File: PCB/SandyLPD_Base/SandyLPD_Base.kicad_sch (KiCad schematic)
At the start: 230 parts, among them J1 Conn_02x02_Odd_Even, J10 Conn_01x10_Pin, J11 Conn_01x03, J2 Conn_01x03, J4 Conn_01x10_Pin, J5 USB_C_Receptacle_USB2.0, J6 USB_C_Receptacle_USB2.0, J7 USB_C_Receptacle_USB2.0, J8 USB_C_Receptacle_USB2.0, J9 Conn_02x02_Odd_Even, SW1 BOOT_ALT, SW2 RESET_ALT, SW3 SW_DIP_x04, SW4 BOOT_ALT, SW5 RESET_ALT, SW6 SW_DIP_x04, U1 NCP1117-3.3_SOT223, U2 NCP1117-3.3_SOT223, U3 RP2040, U4 W25Q128JVPIQ, U5 RP2040, U6 W25Q128JVPIQ, Y1 12MHz, Y2 12MHz

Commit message: ネジ等の3Dモデル追加
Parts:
- H_btm_1, H_btm_2, H_btm_3, H_btm_4, H_btm_5, H_btm_6: footprint locallib:MountingHole_M2_Through-hole_tap_THC-0.8-x-2 -> locallib:MountingHole_M2_Through-hole_tap_THC-0.8-1.0-2
- H_mid_1, H_mid_10, H_mid_11, H_mid_12, H_mid_13, H_mid_14, H_mid_15, H_mid_16, H_mid_17, H_mid_18, H_mid_19, H_mid_2, H_mid_20, H_mid_21, H_mid_22, H_mid_3, H_mid_4, H_mid_5, H_mid_6, H_mid_7, H_mid_8, H_mid_9: footprint locallib:MountingHole_M2_Through-hole_tap_THC-0.8-x-2 -> locallib:MountingHole_M2_Through-hole_tap_THC-0.8-2.0-2
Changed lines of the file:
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@@
 			)
 		)
-		(property "Footprint" "locallib:MountingHole_M2_Through-hole_tap_THC-0.8-x-2"
+		(property "Footprint" "locallib:MountingHole_M2_Through-hole_tap_THC-0.8-2.0-2"
 			(at 196.215 311.785 0)
 			(effects
@@
 			)
 		)
-		(property "Footprint" "locallib:MountingHole_M2_Through-hole_tap_THC-0.8-x-2"
+		(property "Footprint" "locallib:MountingHole_M2_Through-hole_tap_THC-0.8-1.0-2"
 			(at 89.535 311.15 0)
 			(effects
@@
 			)
 		)
-		(property "Footprint" "locallib:MountingHole_M2_Through-hole_tap_THC-0.8-x-2"
+		(property "Footprint" "locallib:MountingHole_M2_Through-hole_tap_THC-0.8-2.0-2"
 			(at 264.795 311.785 0)
 			(effects
@@
 			)
 		)
-		(property "Footprint" "locallib:MountingHole_M2_Through-hole_tap_THC-0.8-x-2"
+		(property "Footprint" "locallib:MountingHole_M2_Through-hole_tap_THC-0.8-2.0-2"
 			(at 347.345 332.105 0)
 			(effects
@@
 			)
 		)
-		(property "Footprint" "locallib:MountingHole_M2_Through-hole_tap_THC-0.8-x-2"
+		(property "Footprint" "locallib:MountingHole_M2_Through-hole_tap_THC-0.8-2.0-2"
 			(at 342.265 311.785 0)
 			(effects
@@
 			)
 		)
-		(property "Footprint" "locallib:MountingHole_M2_Through-hole_tap_THC-0.8-x-2"
+		(property "Footprint" "locallib:MountingHole_M2_Through-hole_tap_THC-0.8-2.0-2"
 			(at 422.275 311.785 0)
 			(effects
@@
 			)
 		)
-		(property "Footprint" "locallib:MountingHole_M2_Through-hole_tap_THC-0.8-x-2"
+		(property "Footprint" "locallib:MountingHole_M2_Through-hole_tap_THC-0.8-2.0-2"
 			(at 422.275 321.945 0)
 			(effects
@@
 			)
 		)
-		(property "Footprint" "locallib:MountingHole_M2_Through-hole_tap_THC-0.8-x-2"
+		(property "Footprint" "locallib:MountingHole_M2_Through-hole_tap_THC-0.8-2.0-2"
 			(at 196.215 321.945 0)
 			(effects
@@
 			)
 		)
-		(property "Footprint" "locallib:MountingHole_M2_Through-hole_tap_THC-0.8-x-2"
+		(property "Footprint" "locallib:MountingHole_M2_Through-hole_tap_THC-0.8-1.0-2"
 			(at 39.37 323.85 0)
 			(effects
@@
 			)
 		)
-		(property "Footprint" "locallib:MountingHole_M2_Through-hole_tap_THC-0.8-x-2"
+		(property "Footprint" "locallib:MountingHole_M2_Through-hole_tap_THC-0.8-1.0-2"
 			(at 100.965 323.85 0)
 			(effects
@@
 			)
 		)
-		(property "Footprint" "locallib:MountingHole_M2_Through-hole_tap_THC-0.8-x-2"
+		(property "Footprint" "locallib:MountingHole_M2_Through-hole_tap_THC-0.8-2.0-2"
 			(at 219.075 321.945 0)
 			(effects
@@
 			)
 		)
-		(property "Footprint" "locallib:MountingHole_M2_Through-hole_tap_THC-0.8-x-2"
+		(property "Footprint" "locallib:MountingHole_M2_Through-hole_tap_THC-0.8-2.0-2"
 			(at 244.475 311.785 0)
 			(effects
@@
 			)
 		)
-		(property "Footprint" "locallib:MountingHole_M2_Through-hole_tap_THC-0.8-x-2"
+		(property "Footprint" "locallib:MountingHole_M2_Through-hole_tap_THC-0.8-2.0-2"
 			(at 283.21 321.945 0)
 			(effects
@@
 			)
 		)
-		(property "Footprint" "locallib:MountingHole_M2_Through-hole_tap_THC-0.8-x-2"
+		(property "Footprint" "locallib:MountingHole_M2_Through-hole_tap_THC-0.8-2.0-2"
 			(at 399.415 311.785 0)
 			(effects
@@
 			)
 		)
-		(property "Footprint" "locallib:MountingHole_M2_Through-hole_tap_THC-0.8-x-2"
+		(property "Footprint" "locallib:MountingHole_M2_Through-hole_tap_THC-0.8-2.0-2"
 			(at 342.265 342.265 0)
 			(effects
@@
 			)
 		)
-		(property "Footprint" "locallib:MountingHole_M2_Through-hole_tap_THC-0.8-x-2"
+		(property "Footprint" "locallib:MountingHole_M2_Through-hole_tap_THC-0.8-1.0-2"
 			(at 10.16 323.85 0)
 			(effects
@@
 			)
 		)
-		(property "Footprint" "locallib:MountingHole_M2_Through-hole_tap_THC-0.8-x-2"
+		(property "Footprint" "locallib:MountingHole_M2_Through-hole_tap_THC-0.8-2.0-2"
 			(at 278.13 332.105 0)
 			(effects
@@
 			)
 		)
-		(property "Footprint" "locallib:MountingHole_M2_Through-hole_tap_THC-0.8-x-2"
+		(property "Footprint" "locallib:MountingHole_M2_Through-hole_tap_THC-0.8-2.0-2"
 			(at 375.285 321.945 0)
 			(effects
@@
 			)
 		)
-		(property "Footprint" "locallib:MountingHole_M2_Through-hole_tap_THC-0.8-x-2"
+		(property "Footprint" "locallib:MountingHole_M2_Through-hole_tap_THC-0.8-2.0-2"
 			(at 219.075 311.785 0)
 			(effects
@@
 			)
 		)
-		(property "Footprint" "locallib:MountingHole_M2_Through-hole_tap_THC-0.8-x-2"
+		(property "Footprint" "locallib:MountingHole_M2_Through-hole_tap_THC-0.8-2.0-2"
 			(at 363.22 311.785 0)
 			(effects
@@
 			)
 		)
-		(property "Footprint" "locallib:MountingHole_M2_Through-hole_tap_THC-0.8-x-2"
+		(property "Footprint" "locallib:MountingHole_M2_Through-hole_tap_THC-0.8-1.0-2"
 			(at 21.59 311.15 0)
 			(effects
@@
 			)
 		)
-		(property "Footprint" "locallib:MountingHole_M2_Through-hole_tap_THC-0.8-x-2"
+		(property "Footprint" "locallib:MountingHole_M2_Through-hole_tap_THC-0.8-2.0-2"
 			(at 399.415 321.945 0)
 			(effects
@@
 			)
 		)
-		(property "Footprint" "locallib:MountingHole_M2_Through-hole_tap_THC-0.8-x-2"
+		(property "Footprint" "locallib:MountingHole_M2_Through-hole_tap_THC-0.8-2.0-2"
 			(at 283.21 342.265 0)
 			(effects
@@
 			)
 		)
-		(property "Footprint" "locallib:MountingHole_M2_Through-hole_tap_THC-0.8-x-2"
+		(property "Footprint" "locallib:MountingHole_M2_Through-hole_tap_THC-0.8-2.0-2"
 			(at 342.265 321.945 0)
 			(effects
@@
 			)
 		)
-		(property "Footprint" "locallib:MountingHole_M2_Through-hole_tap_THC-0.8-x-2"
+		(property "Footprint" "locallib:MountingHole_M2_Through-hole_tap_THC-0.8-1.0-2"
 			(at 71.12 323.85 0)
 			(effects
@@
 			)
 		)
-		(property "Footprint" "locallib:MountingHole_M2_Through-hole_tap_THC-0.8-x-2"
+		(property "Footprint" "locallib:MountingHole_M2_Through-hole_tap_THC-0.8-2.0-2"
 			(at 377.825 311.785 0)
 			(effects
@@
 			)
 		)
-		(property "Footprint" "locallib:MountingHole_M2_Through-hole_tap_THC-0.8-x-2"
+		(property "Footprint" "locallib:MountingHole_M2_Through-hole_tap_THC-0.8-2.0-2"
 			(at 283.21 311.785 0)
 			(effects
@@
 			)
 		)
-		(property "Footprint" "locallib:MountingHole_M2_Through-hole_tap_THC-0.8-x-2"
+		(property "Footprint" "locallib:MountingHole_M2_Through-hole_tap_THC-0.8-2.0-2"
 			(at 247.015 321.945 0)
 			(effects

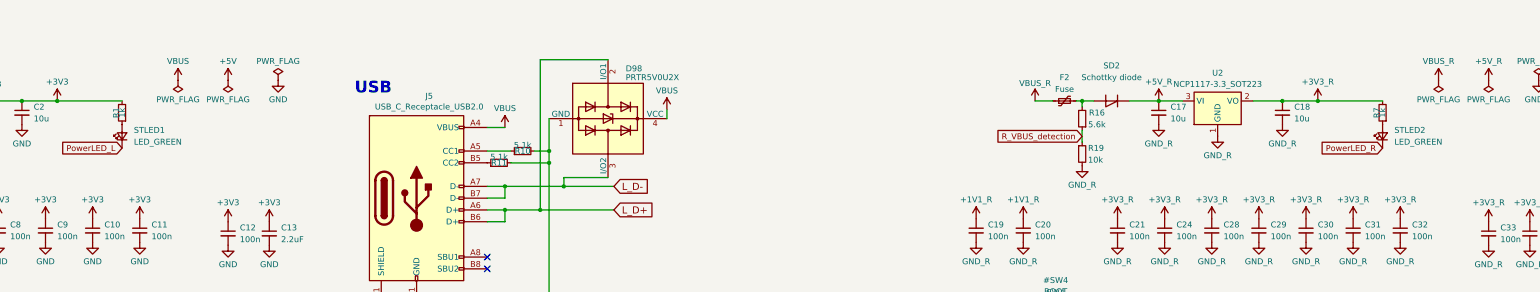
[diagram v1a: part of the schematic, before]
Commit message: DIPスイッチ取り付け前に通電確認できるジャンパを追加。 #42
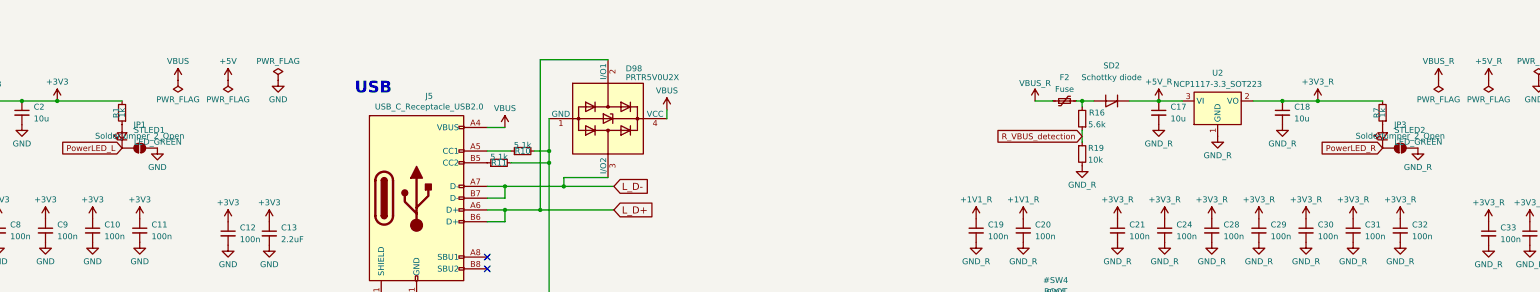
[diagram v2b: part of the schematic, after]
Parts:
- added JP1, JP3: SolderJumper_2_Open, locallib:SolderJumper-2_P1.3mm_Open_RoundedPad1.0x1.5mm_no_Courtyard, symbol Jumper:SolderJumper_2_Open
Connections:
- net GND: now also JP1.2 (B)
- net GND_R: now also JP3.1 (A)
- net PowerLED_L: now also JP1.1 (A)
- net PowerLED_R: now also JP3.2 (B)

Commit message: シルク調整
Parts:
- H_btm_1, H_btm_2, H_btm_3, H_btm_4, H_btm_5, H_btm_6: footprint locallib:MountingHole_M2_Through-hole_tap_THC-0.8-1.0-2 -> locallib:MountingHole_M2_Through-hole_tap_THC-0.8-1.0-2_minimal
- H_mid_1, H_mid_10, H_mid_11, H_mid_12, H_mid_13, H_mid_14, H_mid_15, H_mid_16, H_mid_17, H_mid_18, H_mid_19, H_mid_2, H_mid_20, H_mid_21, H_mid_22, H_mid_3, H_mid_4, H_mid_5, H_mid_6, H_mid_7, H_mid_8, H_mid_9: footprint locallib:MountingHole_M2_Through-hole_tap_THC-0.8-2.0-2 -> locallib:MountingHole_M2_Through-hole_tap_THC-0.8-2.0-2_minimal
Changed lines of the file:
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@@
 			)
 		)
-		(property "Footprint" "locallib:MountingHole_M2_Through-hole_tap_THC-0.8-2.0-2"
+		(property "Footprint" "locallib:MountingHole_M2_Through-hole_tap_THC-0.8-2.0-2_minimal"
 			(at 196.215 311.785 0)
 			(effects
@@
 			)
 		)
-		(property "Footprint" "locallib:MountingHole_M2_Through-hole_tap_THC-0.8-1.0-2"
+		(property "Footprint" "locallib:MountingHole_M2_Through-hole_tap_THC-0.8-1.0-2_minimal"
 			(at 89.535 311.15 0)
 			(effects
@@
 			)
 		)
-		(property "Footprint" "locallib:MountingHole_M2_Through-hole_tap_THC-0.8-2.0-2"
+		(property "Footprint" "locallib:MountingHole_M2_Through-hole_tap_THC-0.8-2.0-2_minimal"
 			(at 264.795 311.785 0)
 			(effects
@@
 			)
 		)
-		(property "Footprint" "locallib:MountingHole_M2_Through-hole_tap_THC-0.8-2.0-2"
+		(property "Footprint" "locallib:MountingHole_M2_Through-hole_tap_THC-0.8-2.0-2_minimal"
 			(at 347.345 332.105 0)
 			(effects
@@
 			)
 		)
-		(property "Footprint" "locallib:MountingHole_M2_Through-hole_tap_THC-0.8-2.0-2"
+		(property "Footprint" "locallib:MountingHole_M2_Through-hole_tap_THC-0.8-2.0-2_minimal"
 			(at 342.265 311.785 0)
 			(effects
@@
 			)
 		)
-		(property "Footprint" "locallib:MountingHole_M2_Through-hole_tap_THC-0.8-2.0-2"
+		(property "Footprint" "locallib:MountingHole_M2_Through-hole_tap_THC-0.8-2.0-2_minimal"
 			(at 422.275 311.785 0)
 			(effects
@@
 			)
 		)
-		(property "Footprint" "locallib:MountingHole_M2_Through-hole_tap_THC-0.8-2.0-2"
+		(property "Footprint" "locallib:MountingHole_M2_Through-hole_tap_THC-0.8-2.0-2_minimal"
 			(at 422.275 321.945 0)
 			(effects
@@
 			)
 		)
-		(property "Footprint" "locallib:MountingHole_M2_Through-hole_tap_THC-0.8-2.0-2"
+		(property "Footprint" "locallib:MountingHole_M2_Through-hole_tap_THC-0.8-2.0-2_minimal"
 			(at 196.215 321.945 0)
 			(effects
@@
 			)
 		)
-		(property "Footprint" "locallib:MountingHole_M2_Through-hole_tap_THC-0.8-1.0-2"
+		(property "Footprint" "locallib:MountingHole_M2_Through-hole_tap_THC-0.8-1.0-2_minimal"
 			(at 39.37 323.85 0)
 			(effects
@@
 			)
 		)
-		(property "Footprint" "locallib:MountingHole_M2_Through-hole_tap_THC-0.8-1.0-2"
+		(property "Footprint" "locallib:MountingHole_M2_Through-hole_tap_THC-0.8-1.0-2_minimal"
 			(at 100.965 323.85 0)
 			(effects
@@
 			)
 		)
-		(property "Footprint" "locallib:MountingHole_M2_Through-hole_tap_THC-0.8-2.0-2"
+		(property "Footprint" "locallib:MountingHole_M2_Through-hole_tap_THC-0.8-2.0-2_minimal"
 			(at 219.075 321.945 0)
 			(effects
@@
 			)
 		)
-		(property "Footprint" "locallib:MountingHole_M2_Through-hole_tap_THC-0.8-2.0-2"
+		(property "Footprint" "locallib:MountingHole_M2_Through-hole_tap_THC-0.8-2.0-2_minimal"
 			(at 244.475 311.785 0)
 			(effects
@@
 			)
 		)
-		(property "Footprint" "locallib:MountingHole_M2_Through-hole_tap_THC-0.8-2.0-2"
+		(property "Footprint" "locallib:MountingHole_M2_Through-hole_tap_THC-0.8-2.0-2_minimal"
 			(at 283.21 321.945 0)
 			(effects
@@
 			)
 		)
-		(property "Footprint" "locallib:MountingHole_M2_Through-hole_tap_THC-0.8-2.0-2"
+		(property "Footprint" "locallib:MountingHole_M2_Through-hole_tap_THC-0.8-2.0-2_minimal"
 			(at 399.415 311.785 0)
 			(effects
@@
 			)
 		)
-		(property "Footprint" "locallib:MountingHole_M2_Through-hole_tap_THC-0.8-2.0-2"
+		(property "Footprint" "locallib:MountingHole_M2_Through-hole_tap_THC-0.8-2.0-2_minimal"
 			(at 342.265 342.265 0)
 			(effects
@@
 			)
 		)
-		(property "Footprint" "locallib:MountingHole_M2_Through-hole_tap_THC-0.8-1.0-2"
+		(property "Footprint" "locallib:MountingHole_M2_Through-hole_tap_THC-0.8-1.0-2_minimal"
 			(at 10.16 323.85 0)
 			(effects
@@
 			)
 		)
-		(property "Footprint" "locallib:MountingHole_M2_Through-hole_tap_THC-0.8-2.0-2"
+		(property "Footprint" "locallib:MountingHole_M2_Through-hole_tap_THC-0.8-2.0-2_minimal"
 			(at 278.13 332.105 0)
 			(effects
@@
 			)
 		)
-		(property "Footprint" "locallib:MountingHole_M2_Through-hole_tap_THC-0.8-2.0-2"
+		(property "Footprint" "locallib:MountingHole_M2_Through-hole_tap_THC-0.8-2.0-2_minimal"
 			(at 375.285 321.945 0)
 			(effects
@@
 			)
 		)
-		(property "Footprint" "locallib:MountingHole_M2_Through-hole_tap_THC-0.8-2.0-2"
+		(property "Footprint" "locallib:MountingHole_M2_Through-hole_tap_THC-0.8-2.0-2_minimal"
 			(at 219.075 311.785 0)
 			(effects
@@
 			)
 		)
-		(property "Footprint" "locallib:MountingHole_M2_Through-hole_tap_THC-0.8-2.0-2"
+		(property "Footprint" "locallib:MountingHole_M2_Through-hole_tap_THC-0.8-2.0-2_minimal"
 			(at 363.22 311.785 0)
 			(effects
@@
 			)
 		)
-		(property "Footprint" "locallib:MountingHole_M2_Through-hole_tap_THC-0.8-1.0-2"
+		(property "Footprint" "locallib:MountingHole_M2_Through-hole_tap_THC-0.8-1.0-2_minimal"
 			(at 21.59 311.15 0)
 			(effects
@@
 			)
 		)
-		(property "Footprint" "locallib:MountingHole_M2_Through-hole_tap_THC-0.8-2.0-2"
+		(property "Footprint" "locallib:MountingHole_M2_Through-hole_tap_THC-0.8-2.0-2_minimal"
 			(at 399.415 321.945 0)
 			(effects
@@
 			)
 		)
-		(property "Footprint" "locallib:MountingHole_M2_Through-hole_tap_THC-0.8-2.0-2"
+		(property "Footprint" "locallib:MountingHole_M2_Through-hole_tap_THC-0.8-2.0-2_minimal"
 			(at 283.21 342.265 0)
 			(effects
@@
 			)
 		)
-		(property "Footprint" "locallib:MountingHole_M2_Through-hole_tap_THC-0.8-2.0-2"
+		(property "Footprint" "locallib:MountingHole_M2_Through-hole_tap_THC-0.8-2.0-2_minimal"
 			(at 342.265 321.945 0)
 			(effects
@@
 			)
 		)
-		(property "Footprint" "locallib:MountingHole_M2_Through-hole_tap_THC-0.8-1.0-2"
+		(property "Footprint" "locallib:MountingHole_M2_Through-hole_tap_THC-0.8-1.0-2_minimal"
 			(at 71.12 323.85 0)
 			(effects
@@
 			)
 		)
-		(property "Footprint" "locallib:MountingHole_M2_Through-hole_tap_THC-0.8-2.0-2"
+		(property "Footprint" "locallib:MountingHole_M2_Through-hole_tap_THC-0.8-2.0-2_minimal"
 			(at 377.825 311.785 0)
 			(effects
@@
 			)
 		)
-		(property "Footprint" "locallib:MountingHole_M2_Through-hole_tap_THC-0.8-2.0-2"
+		(property "Footprint" "locallib:MountingHole_M2_Through-hole_tap_THC-0.8-2.0-2_minimal"
 			(at 283.21 311.785 0)
 			(effects
@@
 			)
 		)
-		(property "Footprint" "locallib:MountingHole_M2_Through-hole_tap_THC-0.8-2.0-2"
+		(property "Footprint" "locallib:MountingHole_M2_Through-hole_tap_THC-0.8-2.0-2_minimal"
 			(at 247.015 321.945 0)
 			(effects
